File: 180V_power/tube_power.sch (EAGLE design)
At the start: 21 parts, among them IC1 NE555D, Q1 IRF740S, Q2 BC546

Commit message: new stuff
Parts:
- removed 7805: 78, iStivi - Transistor-FET-reg:78
- removed Q2: BC546, iStivi - Transistor-FET-reg:BC546A
- added U1: TLV1117-5SOT-223, iStivi - Transistor-FET-reg:TLV1117-5SOT-223
- added U2: BC817, iStivi - Transistor-FET-reg:BC817
- L1: device iStivi - RCLD:INDUCTORTFI0307 -> iStivi - RCLD:INDUCTOR
- Q1: device iStivi - Transistor-FET:IRF740S -> iStivi - Transistor-FET-reg:IRF740S
- R1: value 56K -> 220K; device iStivi - RCLD:RESISTORR1206 -> iStivi - RCLD:RESISTOR0207/10
- R2: value 10K -> 470R; device iStivi - RCLD:RESISTORR1206 -> iStivi - RCLD:RESISTOR0207/10
- R4: value 470R -> 10K; device iStivi - RCLD:RESISTOR0207/10 -> iStivi - RCLD:RESISTORR1206
- R5: value 220K -> 56K; device iStivi - RCLD:RESISTOR0207/10 -> iStivi - RCLD:RESISTORR1206
- renumbered VR1 to R7
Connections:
- net 180V: now also R1.2; no longer R5.2
- net 5V: now also U1.VO; no longer 7805.VO
- net GND: now also R2.1, U1.GND, U2.E; no longer 7805.GND, Q2.E, R4.1
- net N$10: now also U2.B; no longer Q2.B
- net N$26: now also R5.2, U1.VI; no longer 7805.VI, R1.2
- net N$3: now also R5.1, U2.C; no longer Q2.C, R1.1
- net N$4: now also R4.2; no longer R2.2
- net N$5: now also R4.1; no longer R2.1
- net N$8: now also R1.1; no longer R5.1
- net N$9: now also R2.2; no longer R4.2
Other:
- moved on the sheet: R1, R2, R4, R5

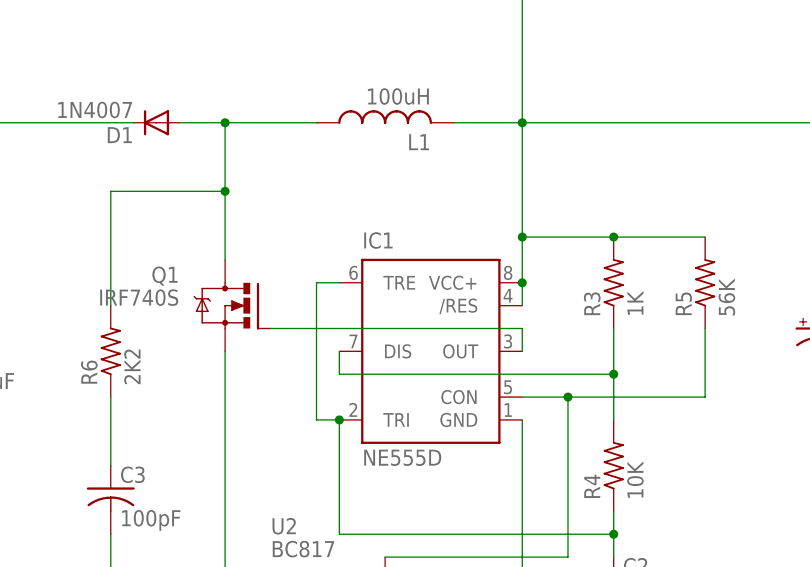
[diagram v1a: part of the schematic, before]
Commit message: made board smaller for production
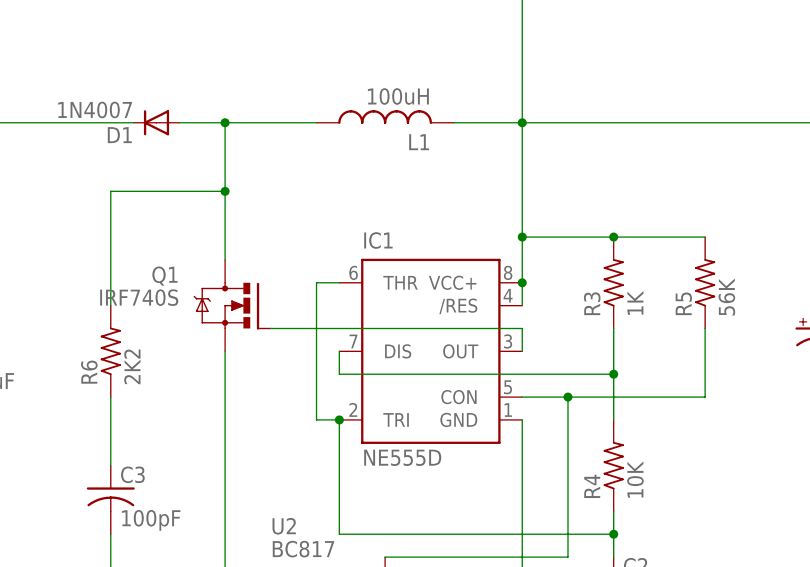
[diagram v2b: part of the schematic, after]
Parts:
- C2, C3: device iStivi - RCLD:CAPACITORC1206K -> iStivi - RCLD:CAPACITORC0805K
- R3, R4, R5, R6: device iStivi - RCLD:RESISTORR1206 -> iStivi - RCLD:RESISTORR0805
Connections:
- net N$5: now also IC1.THR; no longer IC1.TRE
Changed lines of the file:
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@@
 <setting verticaltext="up"/>
 </settings>
-<grid distance="0.05" unitdist="inch" unit="inch" style="lines" multiple="1" display="yes" altdistance="0.025" altunitdist="inch" altunit="inch"/>
+<grid distance="0.1" unitdist="inch" unit="inch" style="lines" multiple="1" display="no" altdistance="0.01" altunitdist="inch" altunit="inch"/>
 <layers>
-<layer number="1" name="Top" color="4" fill="1" visible="yes" active="no"/>
-<layer number="2" name="Route2" color="1" fill="3" visible="yes" active="no"/>
-<layer number="3" name="Route3" color="4" fill="3" visible="yes" active="no"/>
-<layer number="4" name="Route4" color="1" fill="4" visible="yes" active="no"/>
-<layer number="5" name="Route5" color="4" fill="4" visible="yes" active="no"/>
-<layer number="6" name="Route6" color="1" fill="8" visible="yes" active="no"/>
-<layer number="7" name="Route7" color="4" fill="8" visible="yes" active="no"/>
-<layer number="8" name="Route8" color="1" fill="2" visible="yes" active="no"/>
-<layer number="9" name="Route9" color="4" fill="2" visible="yes" active="no"/>
-<layer number="10" name="Route10" color="1" fill="7" visible="yes" active="no"/>
-<layer number="11" name="Route11" color="4" fill="7" visible="yes" active="no"/>
-<layer number="12" name="Route12" color="1" fill="5" visible="yes" active="no"/>
-<layer number="13" name="Route13" color="4" fill="5" visible="yes" active="no"/>
-<layer number="14" name="Route14" color="1" fill="6" visible="yes" active="no"/>
-<layer number="15" name="Route15" color="4" fill="6" visible="yes" active="no"/>
-<layer number="16" name="Bottom" color="1" fill="1" visible="yes" active="no"/>
-<layer number="17" name="Pads" color="2" fill="1" visible="yes" active="no"/>
-<layer number="18" name="Vias" color="2" fill="1" visible="yes" active="no"/>
-<layer number="19" name="Unrouted" color="6" fill="1" visible="yes" active="no"/>
-<layer number="20" name="Dimension" color="15" fill="1" visible="yes" active="no"/>
-<layer number="21" name="tPlace" color="7" fill="1" visible="yes" active="no"/>
-<layer number="22" name="bPlace" color="7" fill="1" visible="yes" active="no"/>
-<layer number="23" name="tOrigins" color="15" fill="1" visible="yes" active="no"/>
-<layer number="24" name="bOrigins" color="15" fill="1" visible="yes" active="no"/>
-<layer number="25" name="tNames" color="7" fill="1" visible="yes" active="no"/>
-<layer number="26" name="bNames" color="7" fill="1" visible="yes" active="no"/>
-<layer number="27" name="tValues" color="7" fill="1" visible="yes" active="no"/>
-<layer number="28" name="bValues" color="7" fill="1" visible="yes" active="no"/>
+<layer number="1" name="Top" color="4" fill="1" visible="no" active="no"/>
+<layer number="2" name="Route2" color="1" fill="3" visible="no" active="no"/>
+<layer number="3" name="Route3" color="4" fill="3" visible="no" active="no"/>
+<layer number="4" name="Route4" color="1" fill="4" visible="no" active="no"/>
+<layer number="5" name="Route5" color="4" fill="4" visible="no" active="no"/>
+<layer number="6" name="Route6" color="1" fill="8" visible="no" active="no"/>
+<layer number="7" name="Route7" color="4" fill="8" visible="no" active="no"/>
+<layer number="8" name="Route8" color="1" fill="2" visible="no" active="no"/>
+<layer number="9" name="Route9" color="4" fill="2" visible="no" active="no"/>
+<layer number="10" name="Route10" color="1" fill="7" visible="no" active="no"/>
+<layer number="11" name="Route11" color="4" fill="7" visible="no" active="no"/>
+<layer number="12" name="Route12" color="1" fill="5" visible="no" active="no"/>
+<layer number="13" name="Route13" color="4" fill="5" visible="no" active="no"/>
+<layer number="14" name="Route14" color="1" fill="6" visible="no" active="no"/>
+<layer number="15" name="Route15" color="4" fill="6" visible="no" active="no"/>
+<layer number="16" name="Bottom" color="1" fill="1" visible="no" active="no"/>
+<layer number="17" name="Pads" color="2" fill="1" visible="no" active="no"/>
+<layer number="18" name="Vias" color="2" fill="1" visible="no" active="no"/>
+<layer number="19" name="Unrouted" color="6" fill="1" visible="no" active="no"/>
+<layer number="20" name="Dimension" color="15" fill="1" visible="no" active="no"/>
+<layer number="21" name="tPlace" color="7" fill="1" visible="no" active="no"/>
+<layer number="22" name="bPlace" color="7" fill="1" visible="no" active="no"/>
+<layer number="23" name="tOrigins" color="15" fill="1" visible="no" active="no"/>
+<layer number="24" name="bOrigins" color="15" fill="1" visible="no" active="no"/>
+<layer number="25" name="tNames" color="7" fill="1" visible="no" active="no"/>
+<layer number="26" name="bNames" color="7" fill="1" visible="no" active="no"/>
+<layer number="27" name="tValues" color="7" fill="1" visible="no" active="no"/>
+<layer number="28" name="bValues" color="7" fill="1" visible="no" active="no"/>
 <layer number="29" name="tStop" color="7" fill="3" visible="no" active="no"/>
 <layer number="30" name="bStop" color="7" fill="6" visible="no" active="no"/>
@@
 <layer number="35" name="tGlue" color="7" fill="4" visible="no" active="no"/>
 <layer number="36" name="bGlue" color="7" fill="5" visible="no" active="no"/>
-<layer number="37" name="tTest" color="7" fill="1" visible="yes" active="no"/>
-<layer number="38" name="bTest" color="7" fill="1" visible="yes" active="no"/>
+<layer number="37" name="tTest" color="7" fill="1" visible="no" active="no"/>
+<layer number="38" name="bTest" color="7" fill="1" visible="no" active="no"/>
 <layer number="39" name="tKeepout" color="4" fill="11" visible="no" active="no"/>
 <layer number="40" name="bKeepout" color="1" fill="11" visible="no" active="no"/>
@@
 <layer number="44" name="Drills" color="7" fill="1" visible="no" active="no"/>
 <layer number="45" name="Holes" color="7" fill="1" visible="no" active="no"/>
-<layer number="46" name="Milling" color="3" fill="1" visible="yes" active="no"/>
-<layer number="47" name="Measures" color="7" fill="1" visible="yes" active="no"/>
-<layer number="48" name="Document" color="7" fill="1" visible="yes" active="no"/>
-<layer number="49" name="Reference" color="7" fill="1" visible="yes" active="no"/>
-<layer number="50" name="dxf" color="7" fill="1" visible="yes" active="no"/>
-<layer number="51" name="tDocu" color="7" fill="1" visible="yes" active="no"/>
-<layer number="52" name="bDocu" color="7" fill="1" visible="yes" active="no"/>
-<layer number="53" name="tGND_GNDA" color="7" fill="9" visible="yes" active="no"/>
-<layer number="54" name="bGND_GNDA" color="1" fill="9" visible="yes" active="no"/>
-<layer number="56" name="wert" color="7" fill="1" visible="yes" active="no"/>
+<layer number="46" name="Milling" color="3" fill="1" visible="no" active="no"/>
+<layer number="47" name="Measures" color="7" fill="1" visible="no" active="no"/>
+<layer number="48" name="Document" color="7" fill="1" visible="no" active="no"/>
+<layer number="49" name="Reference" color="7" fill="1" visible="no" active="no"/>
+<layer number="50" name="dxf" color="7" fill="1" visible="no" active="no"/>
+<layer number="51" name="tDocu" color="7" fill="1" visible="no" active="no"/>
+<layer number="52" name="bDocu" color="7" fill="1" visible="no" active="no"/>
+<layer number="53" name="tGND_GNDA" color="7" fill="9" visible="no" active="no"/>
+<layer number="54" name="bGND_GNDA" color="1" fill="9" visible="no" active="no"/>
+<layer number="56" name="wert" color="7" fill="1" visible="no" active="no"/>
 <layer number="91" name="Nets" color="2" fill="1" visible="yes" active="yes"/>
 <layer number="92" name="Busses" color="1" fill="1" visible="yes" active="yes"/>
@@
 <part name="C4" library="iStivi - RCLD" deviceset="CAPACITOR_POL" device="E3.5-8" value="2.2uF"/>
 <part name="C1" library="iStivi - RCLD" deviceset="CAPACITOR_POL" device="E5-10.5" value="330uF"/>
-<part name="R5" library="iStivi - RCLD" deviceset="RESISTOR" device="R1206" value="56K"/>
-<part name="R4" library="iStivi - RCLD" deviceset="RESISTOR" device="R1206" value="10K"/>
-<part name="R3" library="iStivi - RCLD" deviceset="RESISTOR" device="R1206" value="1K"/>
+<part name="R5" library="iStivi - RCLD" deviceset="RESISTOR" device="R0805" value="56K"/>
+<part name="R4" library="iStivi - RCLD" deviceset="RESISTOR" device="R0805" value="10K"/>
+<part name="R3" library="iStivi - RCLD" deviceset="RESISTOR" device="R0805" value="1K"/>
 <part name="R1" library="iStivi - RCLD" deviceset="RESISTOR" device="0207/10" value="220K"/>
 <part name="R2" library="iStivi - RCLD" deviceset="RESISTOR" device="0207/10" value="470R"/>
-<part name="R6" library="iStivi - RCLD" deviceset="RESISTOR" device="R1206" value="2K2"/>
-<part name="C3" library="iStivi - RCLD" deviceset="CAPACITOR" device="C1206K" value="100pF"/>
-<part name="C2" library="iStivi - RCLD" deviceset="CAPACITOR" device="C1206K" value="2n2"/>
+<part name="R6" library="iStivi - RCLD" deviceset="RESISTOR" device="R0805" value="2K2"/>
+<part name="C3" library="iStivi - RCLD" deviceset="CAPACITOR" device="C0805K" value="100pF"/>
+<part name="C2" library="iStivi - RCLD" deviceset="CAPACITOR" device="C0805K" value="2n2"/>
 <part name="GND1" library="iStivi - Supply" deviceset="GND" device=""/>
 <part name="180V" library="iStivi - Header-Connector" deviceset="M02" device="PTH"/>
@@
 <wire x1="58.42" y1="25.4" x2="58.42" y2="40.64" width="0.1524" layer="91"/>
 <junction x="60.96" y="25.4"/>
-<pinref part="IC1" gate="G$1" pin="TRE"/>
+<pinref part="IC1" gate="G$1" pin="THR"/>
 <wire x1="58.42" y1="40.64" x2="60.96" y2="40.64" width="0.1524" layer="91"/>
 <pinref part="C2" gate="G$1" pin="1"/>

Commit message: board almost final
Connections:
- net N$1 renamed OUT
- net N$10 renamed VAR
- net N$2 renamed R6
- net N$26 renamed VCC
- net N$3 renamed CON
- net N$4 renamed DIS
- net N$5 renamed THR
- net N$6 renamed L1
- net N$8 renamed R1
- net N$9 renamed R2
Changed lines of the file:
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@@
 <part name="Q1" library="iStivi - Transistor-FET-reg" deviceset="IRF740" device="S"/>
 <part name="R7" library="iStivi - RCLD" deviceset="TRIM_POT" device="CA6V" value="1K"/>
+<part name="P+1" library="iStivi - Supply" deviceset="VCC" device=""/>
 </parts>
 <sheets>
@@
 <instance part="Q1" gate="G$1" x="50.8" y="38.1" rot="MR0"/>
 <instance part="R7" gate="G$1" x="0" y="17.78"/>
+<instance part="P+1" gate="VCC" x="88.9" y="66.04"/>
 </instances>
 <busses>
 </busses>
 <nets>
-<net name="N$1" class="0">
+<net name="OUT" class="0">
 <segment>
 <pinref part="IC1" gate="G$1" pin="OUT"/>
@@
 </segment>
 </net>
-<net name="N$2" class="0">
+<net name="R6" class="0">
 <segment>
 <pinref part="C3" gate="G$1" pin="1"/>
@@
 </segment>
 </net>
-<net name="N$4" class="0">
+<net name="DIS" class="0">
 <segment>
 <pinref part="R3" gate="G$1" pin="1"/>
@@
 </segment>
 </net>
-<net name="N$3" class="0">
+<net name="CON" class="0">
 <segment>
 <pinref part="IC1" gate="G$1" pin="CON"/>
@@
 </segment>
 </net>
-<net name="N$5" class="0">
+<net name="THR" class="0">
 <segment>
 <pinref part="IC1" gate="G$1" pin="TRI"/>
@@
 </segment>
 </net>
-<net name="N$6" class="0">
+<net name="L1" class="0">
 <segment>
 <wire x1="48.26" y1="43.18" x2="48.26" y2="50.8" width="0.1524" layer="91"/>
@@
 </segment>
 </net>
-<net name="N$8" class="0">
+<net name="R1" class="0">
 <segment>
 <pinref part="R1" gate="G$1" pin="1"/>
@@
 </segment>
 </net>
-<net name="N$9" class="0">
+<net name="R2" class="0">
 <segment>
 <pinref part="R2" gate="G$1" pin="2"/>
@@
 </segment>
 </net>
-<net name="N$10" class="0">
+<net name="VAR" class="0">
 <segment>
 <wire x1="5.08" y1="17.78" x2="5.08" y2="5.08" width="0.1524" layer="91"/>
@@
 </segment>
 </net>
-<net name="N$26" class="0">
+<net name="5V" class="2">
+<segment>
+<pinref part="C5" gate="G$1" pin="+"/>
+<wire x1="157.48" y1="55.88" x2="162.56" y2="55.88" width="0.1524" layer="91"/>
+<pinref part="5V" gate="G$1" pin="1"/>
+<wire x1="177.8" y1="55.88" x2="162.56" y2="55.88" width="0.1524" layer="91"/>
+<junction x="162.56" y="55.88"/>
+<pinref part="U1" gate="G$1" pin="VO"/>
+</segment>
+</net>
+<net name="VCC" class="0">
 <segment>
 <pinref part="IC1" gate="G$1" pin="VCC+"/>
@@
 <pinref part="C1" gate="G$1" pin="+"/>
 <wire x1="114.3" y1="38.1" x2="114.3" y2="58.42" width="0.1524" layer="91"/>
-<wire x1="114.3" y1="58.42" x2="81.28" y2="58.42" width="0.1524" layer="91"/>
+<wire x1="114.3" y1="58.42" x2="88.9" y2="58.42" width="0.1524" layer="91"/>
 <pinref part="IC1" gate="G$1" pin="/RES"/>
+<wire x1="88.9" y1="58.42" x2="81.28" y2="58.42" width="0.1524" layer="91"/>
 <wire x1="81.28" y1="38.1" x2="81.28" y2="40.64" width="0.1524" layer="91"/>
 <junction x="81.28" y="40.64"/>
@@
 <pinref part="U1" gate="G$1" pin="VI"/>
 <pinref part="L1" gate="G$1" pin="2"/>
-</segment>
-</net>
-<net name="5V" class="2">
-<segment>
-<pinref part="C5" gate="G$1" pin="+"/>
-<wire x1="157.48" y1="55.88" x2="162.56" y2="55.88" width="0.1524" layer="91"/>
-<pinref part="5V" gate="G$1" pin="1"/>
-<wire x1="177.8" y1="55.88" x2="162.56" y2="55.88" width="0.1524" layer="91"/>
-<junction x="162.56" y="55.88"/>
-<pinref part="U1" gate="G$1" pin="VO"/>
-</segment>
-</net>
+<pinref part="P+1" gate="VCC" pin="VCC"/>
+<wire x1="88.9" y1="63.5" x2="88.9" y2="58.42" width="0.1524" layer="91"/>
+<junction x="88.9" y="58.42"/>
+</segment>
+</net>

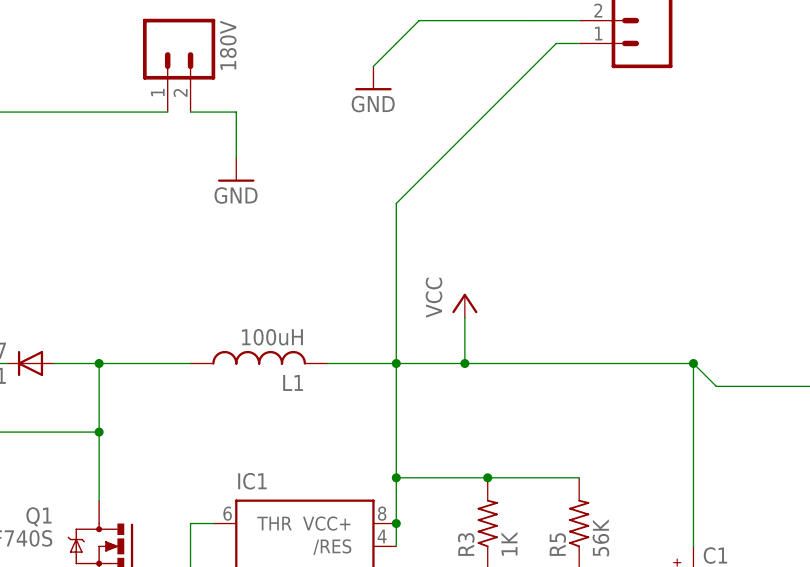
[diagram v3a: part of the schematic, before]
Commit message: added protection diode
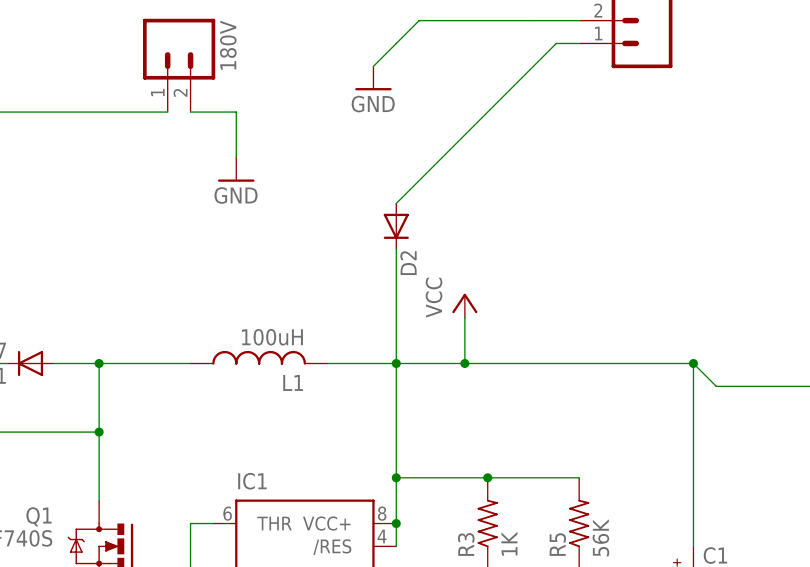
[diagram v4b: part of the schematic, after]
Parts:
- added D2: (no value), iStivi - RCLD:DIODESMA
- C4: device iStivi - RCLD:CAPACITOR_POLE3.5-8 -> iStivi - RCLD:CAPACITOR_POLE5-10.5
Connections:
- new net N$1: D2.A, VIN.1
- net VCC: now also D2.C; no longer VIN.1

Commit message: new format
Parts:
- 180V, 5V, VIN: device iStivi - Header-Connector:M02PTH -> iStivi - Header-Connector:M023.5MM
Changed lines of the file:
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@@
 <part name="C2" library="iStivi - RCLD" deviceset="CAPACITOR" device="C0805K" value="2n2"/>
 <part name="GND1" library="iStivi - Supply" deviceset="GND" device=""/>
-<part name="180V" library="iStivi - Header-Connector" deviceset="M02" device="PTH"/>
+<part name="180V" library="iStivi - Header-Connector" deviceset="M02" device="3.5MM"/>
 <part name="GND2" library="iStivi - Supply" deviceset="GND" device=""/>
 <part name="GND3" library="iStivi - Supply" deviceset="GND" device=""/>
-<part name="VIN" library="iStivi - Header-Connector" deviceset="M02" device="PTH"/>
-<part name="5V" library="iStivi - Header-Connector" deviceset="M02" device="PTH"/>
+<part name="VIN" library="iStivi - Header-Connector" deviceset="M02" device="3.5MM"/>
+<part name="5V" library="iStivi - Header-Connector" deviceset="M02" device="3.5MM"/>
 <part name="C5" library="iStivi - RCLD" deviceset="CAPACITOR_POL" device="E2-5" value="10uF"/>
 <part name="U1" library="iStivi - Transistor-FET-reg" deviceset="TLV1117-5" device="SOT-223"/>
